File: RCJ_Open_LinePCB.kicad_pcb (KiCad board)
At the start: 4 copper layers, 175 x 166.9 mm, 199 parts, among them J1 Conn_01x12

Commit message: Completed Orientation
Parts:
- D1, D10, D11, D12, D13, D14, D15, D16, D17, D18, D19, D2, D20, D21, D22, D23, D24, D25, D26, D27, D28, D29, D3, D30, D31, D32, D33, D34, D35, D36, D37, D38, D39, D4, D40, D41, D42, D43, D44, D45, D46, D47, D48, D49, D5, D50, D51, D52, D53, D54, D55, D56, D57, D58, D59, D6, D60, D61, D62, D63, D64, D65, D66, D67, D68, D69, D7, D70, D71, D72, D73, D74, D75, D76, D77, D78, D79, D8, D80, D81, D82, D83, D84, D85, D86, D87, D88, D89, D9, D90, D91, D92, D93, D94, D95, D96, R1, R10, R11, R12, R13, R14, R15, R16, R17, R18, R19, R2, R20, R21, R22, R23, R24, R25, R26, R27, R28, R29, R3, R30, R31, R32, R33, R34, R35, R36, R37, R38, R39, R4, R40, R41, R42, R43, R44, R45, R46, R47, R48, R49, R5, R50, R51, R52, R53, R54, R55, R56, R57, R58, R59, R6, R60, R61, R62, R63, R64, R65, R66, R67, R68, R69, R7, R70, R71, R72, R73, R74, R75, R76, R77, R78, R79, R8, R80, R81, R82, R83, R84, R85, R86, R87, R88, R89, R9, R90, R91, R92, R93, R94, R95, R96: moved to B.Cu
- moved D24 175.1 mm to (-87.6, 1.51), turned to -179.013 degrees
- moved R7 175.1 mm to (-87.6, -1.58), turned to 178.965 degrees
- moved R86 174.9 mm to (-87.5, 4.59), turned to -176.99 degrees
- moved D39 174.9 mm to (87.4, 0.00)
- moved D76 174.9 mm to (-87.5, -4.67), turned to 176.943 degrees
- moved R47 174.8 mm to (87.3, -3.09), turned to 2.02227 degrees
- moved R55 174.8 mm to (87.3, 3.09), turned to -2.02227 degrees
- moved D70 174.5 mm to (-87.3, 7.67), turned to -174.968 degrees
- moved D63 174.4 mm to (87.2, 6.17), turned to -4.04455 degrees
- moved D64 174.4 mm to (87.2, -6.17), turned to 4.04455 degrees
- moved R91 174.4 mm to (-87.3, -7.75), turned to 174.92 degrees
- moved R46 173.9 mm to (86.9, 9.25), turned to -6.06682 degrees
- moved R50 173.9 mm to (86.9, -9.25), turned to 6.06682 degrees
- moved R8 173.8 mm to (-87.0, 10.7), turned to -172.946 degrees
- moved D23 173.8 mm to (-87.0, -10.8), turned to 172.898 degrees
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
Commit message: Fixed Corner Cases
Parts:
- turned D11 to 69.3854 degrees
- turned D38 to 110.615 degrees
- turned D95 to 128.83 degrees
- turned D96 to -53.0228 degrees
- turned R15 to -129.757 degrees
- turned R49 to 170.796 degrees
- turned R64 to 142 degrees
- turned R65 to 38 degrees

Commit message: Completed Routing (No MCP)
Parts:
- moved R100 327.9 mm to (-77.5, -10.2)
- moved R101 327.9 mm to (-77.5, -7.23)
- moved R102 327.9 mm to (-77.5, -4.28)
- moved R97 327.9 mm to (-77.5, -19.0)
- moved R98 327.9 mm to (-77.5, -16.1)
- moved R99 327.9 mm to (-77.5, -13.1)
- moved J1 322.5 mm to (-66.2, -18.3)
- moved D61 1.16 mm to (78.6, 22.1), turned to 162.828 degrees
- moved R64 0.71 mm to (81.1, 25.6)
- moved D8 0.55 mm to (-77.5, 22.5)
- moved D77 0.49 mm to (78.3, -23.2), turned to -90 degrees
- moved R94 0.49 mm to (-77.4, -22.6)
- moved D36 0.48 mm to (84.2, -24.0)
- moved D26 0.41 mm to (-83.0, 25.7)
- moved R5 0.41 mm to (-82.9, -25.7)
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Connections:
- R37 pad 1: unconnected-(R37-Pad1) -> 3.3V
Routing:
- net 3.3V: track 0.00 -> 852.9 mm
- net GND: track 0.00 -> 827.6 mm, vias 0 -> 48
- net CS1: track 0.00 -> 21.0 mm, vias 0 -> 1
- net Net-(D61-A): track 0.00 -> 19.1 mm
- net Net-(D86-A): track 0.00 -> 15.3 mm
- net Net-(D85-A): track 0.00 -> 15.1 mm
- net Net-(D91-A): track 0.00 -> 15.0 mm
- net CS2: track 0.00 -> 14.7 mm, vias 0 -> 1
- net CS5: track 0.00 -> 14.6 mm, vias 0 -> 1
- net Net-(D31-A): track 0.00 -> 14.4 mm
- net CS3: track 0.00 -> 12.4 mm, vias 0 -> 1
- net Net-(D90-A): track 0.00 -> 11.3 mm
- net Net-(D77-A): track 0.00 -> 11.3 mm
- net Net-(D89-A): track 0.00 -> 11.2 mm
- net Net-(D93-A): track 0.00 -> 11.1 mm
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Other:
- board size 175 x 166.9 mm -> 180 x 171.9 mm

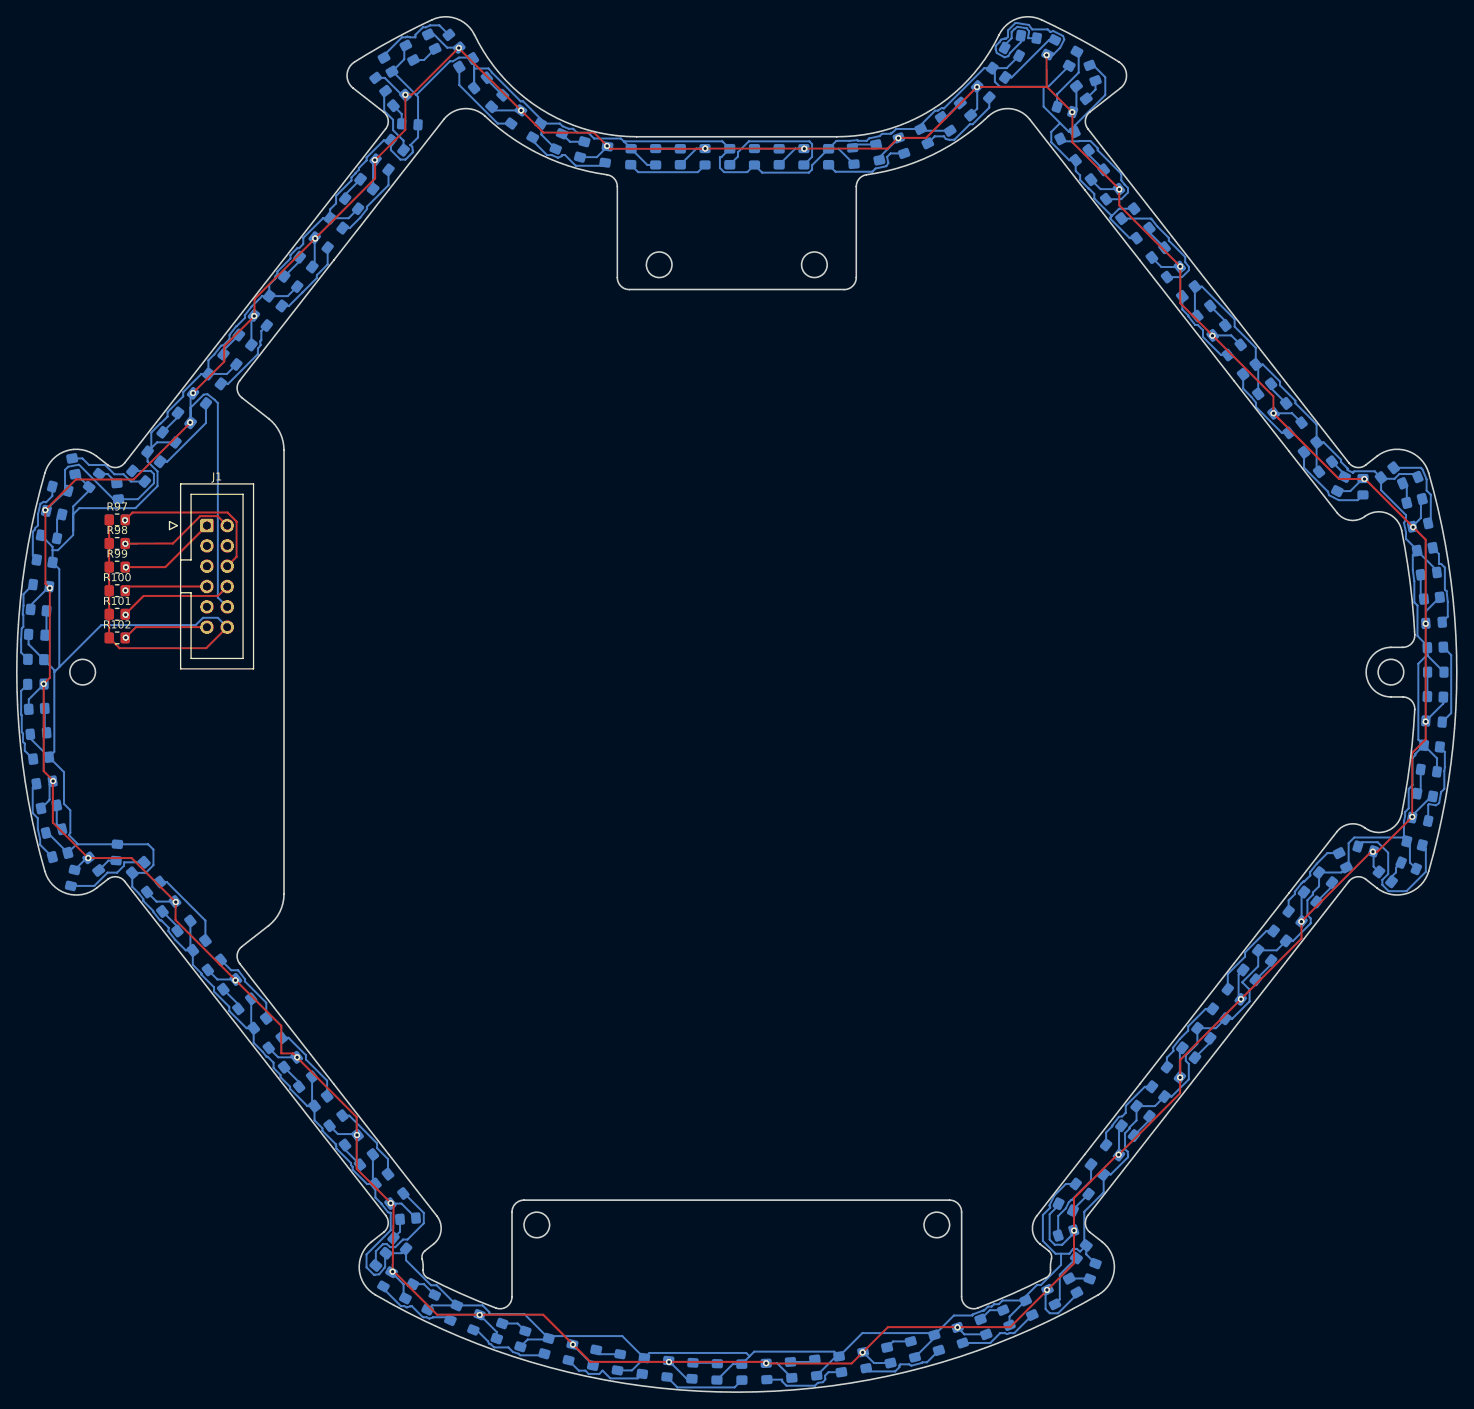
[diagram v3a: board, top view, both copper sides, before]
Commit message: Finished Routing
Routed all channel pins, all ADC pins, and header pins
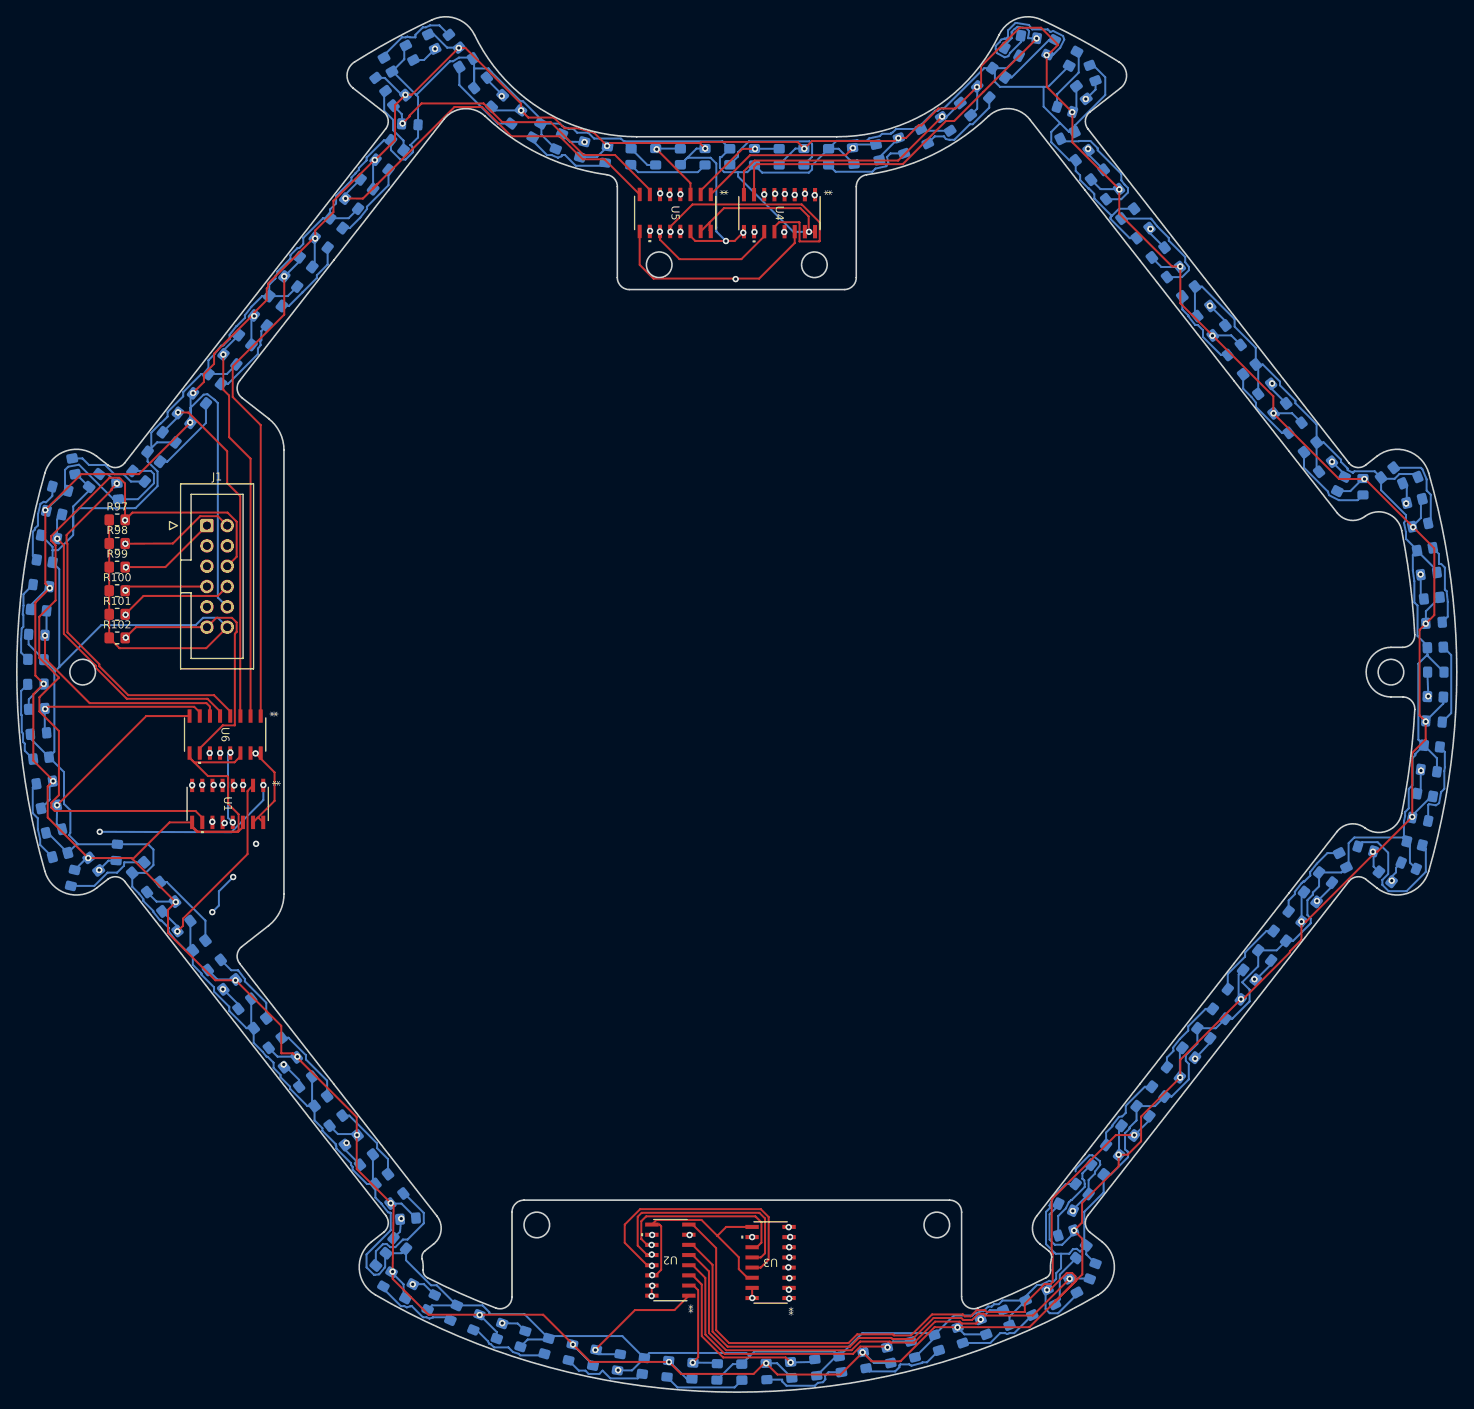
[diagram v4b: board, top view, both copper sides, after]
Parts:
- added U1: MCP3008, MCP3008:SOIC16-N_MC_MCH-L, F.Cu at (-63.6, 16.5)
- added U2: MCP3008, MCP3008:SOIC16-N_MC_MCH-L, F.Cu at (-8.30, 73.5)
- added U3: MCP3008, MCP3008:SOIC16-N_MC_MCH-L, F.Cu at (4.22, 73.8)
- added U4: MCP3008, MCP3008:SOIC16-N_MC_MCH-L, F.Cu at (5.33, -57.4)
- added U5: MCP3008, MCP3008:SOIC16-N_MC_MCH-L, F.Cu at (-7.70, -57.4)
- added U6: MCP3008, MCP3008:SOIC16-N_MC_MCH-L, F.Cu at (-64.0, 7.80)
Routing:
- net SCK1: track 0.00 -> 348.7 mm, vias 0 -> 5
- net MOSI: track 0.00 -> 334.0 mm, vias 0 -> 4
- net MISO: track 0.00 -> 324.2 mm, vias 0 -> 5
- net GND: track 827.6 -> 1004.6 mm, vias 48 -> 52
- net CS3: track 12.4 -> 176.3 mm, vias 1 -> 2
- net Ch24: track 2.66 -> 165.8 mm, vias 0 -> 2
- net Ch23: track 3.19 -> 161.7 mm, vias 0 -> 2
- net CS2: track 14.7 -> 159.8 mm, vias 1 -> 2
- net Ch22: track 3.06 -> 142.3 mm, vias 0 -> 2
- net CS4: track 10.4 -> 137.7 mm, vias 1 -> 2
- net Ch21: track 3.21 -> 130.2 mm, vias 0 -> 2
- net CS5: track 14.6 -> 138.8 mm, vias 1 -> 2
- net Ch20: track 2.89 -> 116.6 mm, vias 0 -> 2
- net Ch19: track 3.21 -> 106.4 mm, vias 0 -> 2
- net Ch18: track 3.21 -> 97.8 mm, vias 0 -> 2
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
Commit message: Moved To Page
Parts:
- moved R30 139.8 mm to (85.0, 180.4)
- moved D1 139.8 mm to (33.7, 126.4)
- moved D10 139.8 mm to (153.6, 149.6)
- moved D11 139.8 mm to (147.3, 169.6)
- moved D12 139.8 mm to (112.7, 181.6)
- moved D13 139.8 mm to (136.5, 175.4)
- moved D14 139.8 mm to (58.5, 31.3)
- moved D15 139.8 mm to (88.1, 181.0)
- moved D16 139.8 mm to (100.3, 182.1)
- moved D17 139.8 mm to (124.8, 179.3)
- moved D18 139.8 mm to (50.8, 41.0)
- moved D19 139.8 mm to (43.2, 50.7)
- moved D2 139.8 mm to (41.3, 136.1)
- moved D20 139.8 mm to (35.6, 60.5)
- moved D21 139.8 mm to (28.0, 70.2)
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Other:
- board text added: "Line PCB"

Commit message: Added Labels
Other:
- board text added: "1"
- board text added: "2/12/2024"
- board text added: "Team Elite"
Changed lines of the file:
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@@
   (gr_line (start 164.942533 131.105272) (end 153.176926 146.164564)
     (stroke (width 0.2) (type solid)) (layer "Edge.Cuts"))
+  (gr_text "Team Elite" (at 178.42 170.97) (layer "User.1")
+    (effects (font (size 3 3) (thickness 0.15)) (justify left bottom))
+  )
   (gr_text "Line PCB" (at 186.45 190.39) (layer "User.1")
     (effects (font (size 1.5 1.5) (thickness 0.3) bold) (justify left bottom))
   )
+  (gr_text "2/12/2024" (at 206.51 193.7) (layer "User.1")
+    (effects (font (size 1 1) (thickness 0.15)) (justify left bottom))
+  )
+  (gr_text "1" (at 268.29 193.83) (layer "User.1")
+    (effects (font (size 1 1) (thickness 0.15)) (justify left bottom))
+  )
   (segment (start 59.57 161.06) (end 59.54 161.06) (width 0.25) (layer "F.Cu") (net 1))

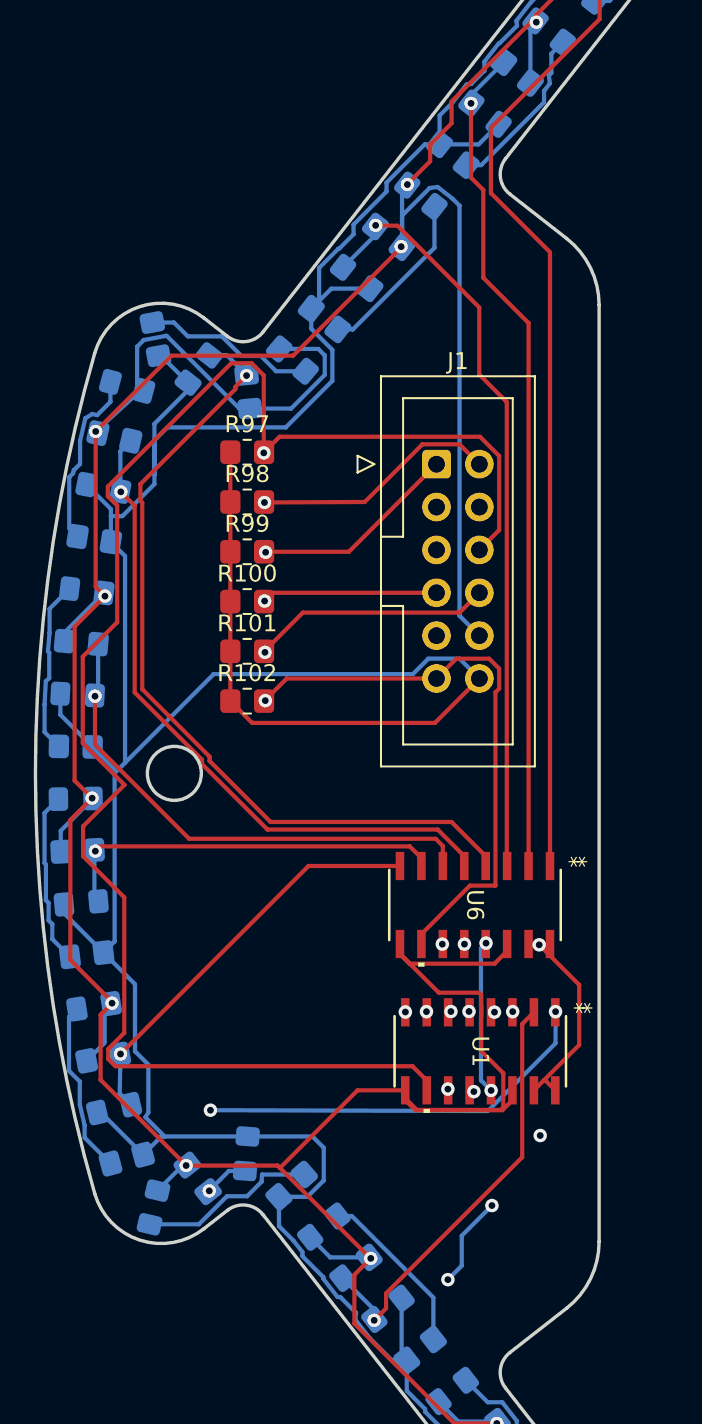
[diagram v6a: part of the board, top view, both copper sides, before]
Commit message: Flipped First 2 MCP
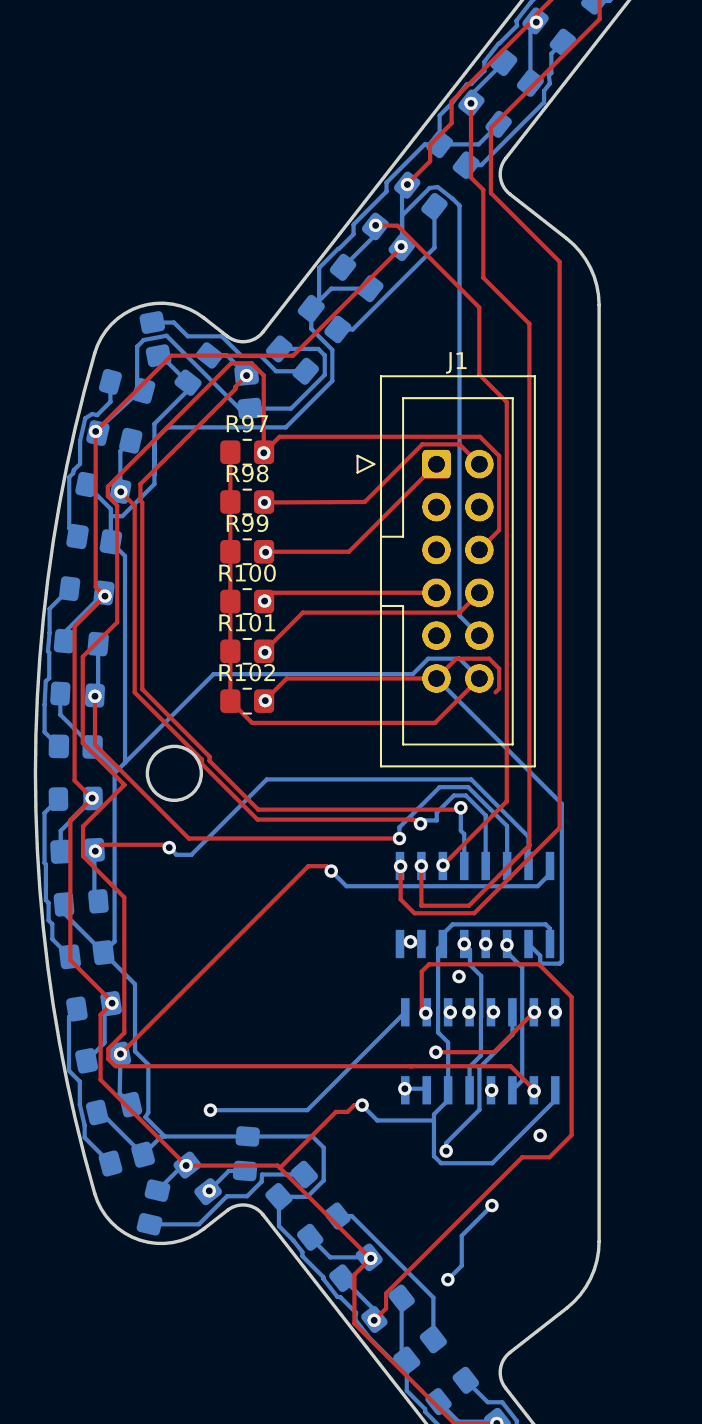
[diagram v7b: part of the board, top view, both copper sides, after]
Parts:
- U1, U6: moved to B.Cu
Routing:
- net Ch2: track 25.5 -> 40.8 mm, vias 1 -> 2
- net Ch41: track 62.3 -> 74.2 mm, vias 1 -> 2
- net Ch47: track 23.4 -> 34.3 mm, vias 1 -> 2
- net Ch48: track 24.5 -> 34.7 mm, vias 1 -> 2
- net Ch1: track 31.6 -> 21.5 mm, vias 3 -> 2
- net Ch42: track 49.9 -> 59.3 mm, vias 1 -> 2
- net MOSI: track 334.0 -> 342.8 mm
- net Ch8: track 97.3 -> 88.7 mm
- net Ch46: track 30.4 -> 38.0 mm, vias 1 -> 2
- net CS1: track 96.5 -> 102.9 mm, vias 1 -> 2
- net CS6: track 34.4 -> 39.4 mm
- net Ch45: track 39.8 -> 44.5 mm, vias 1 -> 2
- net Ch7: track 81.3 -> 86.1 mm, vias 2 -> 3
- net Ch4: track 47.0 -> 42.4 mm
- net MISO: track 324.2 -> 321.2 mm
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
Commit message: rerouting
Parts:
- U2, U3: moved to B.Cu
- turned U2 to 0 degrees
- turned U3 to 0 degrees
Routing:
- net CS3: track 176.3 -> 201.1 mm
- net Ch16: track 89.2 -> 102.4 mm, vias 1 -> 2
- net Ch14: track 64.4 -> 75.4 mm, vias 1 -> 2
- net Ch15: track 96.0 -> 85.2 mm
- net SCK1: track 348.3 -> 338.8 mm, vias 4 -> 5
- net Ch13: track 51.2 -> 60.5 mm, vias 1 -> 2
- net Ch12: track 37.3 -> 44.6 mm, vias 1 -> 2
- net CS2: track 159.8 -> 166.0 mm
- net Ch20: track 116.6 -> 122.5 mm
- net GND: track 1001.7 -> 1007.6 mm, vias 53 -> 56
- net Ch11: track 24.2 -> 29.5 mm, vias 1 -> 2
- net Ch19: track 106.4 -> 111.5 mm
- net Ch18: track 97.8 -> 102.9 mm
- net Ch21: track 130.2 -> 134.9 mm
- net Ch22: track 142.3 -> 146.9 mm
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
